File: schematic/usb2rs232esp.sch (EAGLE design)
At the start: 16 parts, among them IC2 FT232RL

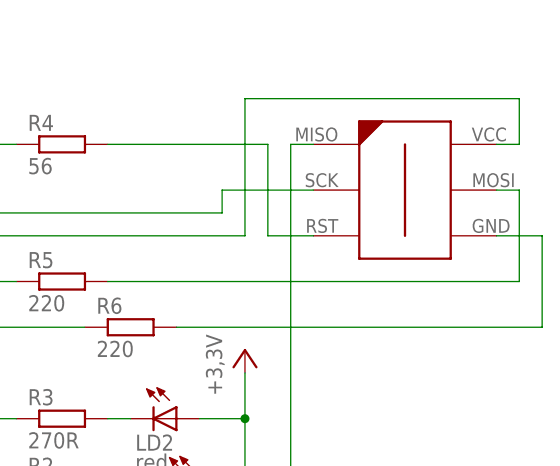
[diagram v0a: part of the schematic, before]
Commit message: improved lables
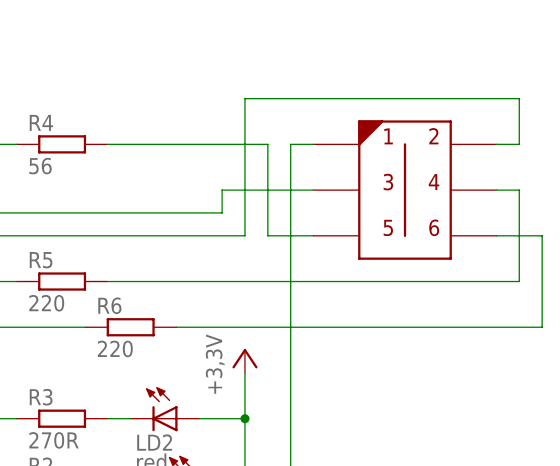
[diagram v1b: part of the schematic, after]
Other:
- note added: "1"
- note added: "2"
- note added: "3"
- note added: "4"
- note added: "5"
- note added: "6"
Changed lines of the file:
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@@
 <grid distance="0.1" unitdist="inch" unit="inch" style="lines" multiple="1" display="no" altdistance="0.01" altunitdist="inch" altunit="inch"/>
 <layers>
-<layer number="1" name="Top" color="4" fill="1" visible="yes" active="no"/>
-<layer number="2" name="Route2" color="3" fill="3" visible="yes" active="no"/>
-<layer number="3" name="Route3" color="5" fill="3" visible="yes" active="no"/>
-<layer number="4" name="Route4" color="1" fill="4" visible="yes" active="no"/>
-<layer number="5" name="Route5" color="4" fill="4" visible="yes" active="no"/>
-<layer number="6" name="Route6" color="1" fill="8" visible="yes" active="no"/>
-<layer number="7" name="Route7" color="4" fill="8" visible="yes" active="no"/>
-<layer number="8" name="Route8" color="1" fill="2" visible="yes" active="no"/>
-<layer number="9" name="Route9" color="4" fill="2" visible="yes" active="no"/>
-<layer number="10" name="Route10" color="1" fill="7" visible="yes" active="no"/>
-<layer number="11" name="Route11" color="4" fill="7" visible="yes" active="no"/>
-<layer number="12" name="Route12" color="1" fill="5" visible="yes" active="no"/>
-<layer number="13" name="Route13" color="4" fill="5" visible="yes" active="no"/>
-<layer number="14" name="Route14" color="1" fill="6" visible="yes" active="no"/>
-<layer number="15" name="Route15" color="4" fill="6" visible="yes" active="no"/>
-<layer number="16" name="Bottom" color="1" fill="1" visible="yes" active="no"/>
-<layer number="17" name="Pads" color="2" fill="1" visible="yes" active="no"/>
-<layer number="18" name="Vias" color="2" fill="1" visible="yes" active="no"/>
-<layer number="19" name="Unrouted" color="6" fill="1" visible="yes" active="no"/>
-<layer number="20" name="Dimension" color="15" fill="1" visible="yes" active="no"/>
-<layer number="21" name="tPlace" color="7" fill="1" visible="yes" active="no"/>
-<layer number="22" name="bPlace" color="7" fill="1" visible="yes" active="no"/>
-<layer number="23" name="tOrigins" color="15" fill="1" visible="yes" active="no"/>
-<layer number="24" name="bOrigins" color="15" fill="1" visible="yes" active="no"/>
-<layer number="25" name="tNames" color="7" fill="1" visible="yes" active="no"/>
-<layer number="26" name="bNames" color="7" fill="1" visible="yes" active="no"/>
-<layer number="27" name="tValues" color="7" fill="1" visible="yes" active="no"/>
-<layer number="28" name="bValues" color="7" fill="1" visible="yes" active="no"/>
+<layer number="1" name="Top" color="4" fill="1" visible="no" active="no"/>
+<layer number="2" name="Route2" color="3" fill="3" visible="no" active="no"/>
+<layer number="3" name="Route3" color="5" fill="3" visible="no" active="no"/>
+<layer number="4" name="Route4" color="1" fill="4" visible="no" active="no"/>
+<layer number="5" name="Route5" color="4" fill="4" visible="no" active="no"/>
+<layer number="6" name="Route6" color="1" fill="8" visible="no" active="no"/>
+<layer number="7" name="Route7" color="4" fill="8" visible="no" active="no"/>
+<layer number="8" name="Route8" color="1" fill="2" visible="no" active="no"/>
+<layer number="9" name="Route9" color="4" fill="2" visible="no" active="no"/>
+<layer number="10" name="Route10" color="1" fill="7" visible="no" active="no"/>
+<layer number="11" name="Route11" color="4" fill="7" visible="no" active="no"/>
+<layer number="12" name="Route12" color="1" fill="5" visible="no" active="no"/>
+<layer number="13" name="Route13" color="4" fill="5" visible="no" active="no"/>
+<layer number="14" name="Route14" color="1" fill="6" visible="no" active="no"/>
+<layer number="15" name="Route15" color="4" fill="6" visible="no" active="no"/>
+<layer number="16" name="Bottom" color="1" fill="1" visible="no" active="no"/>
+<layer number="17" name="Pads" color="2" fill="1" visible="no" active="no"/>
+<layer number="18" name="Vias" color="2" fill="1" visible="no" active="no"/>
+<layer number="19" name="Unrouted" color="6" fill="1" visible="no" active="no"/>
+<layer number="20" name="Dimension" color="15" fill="1" visible="no" active="no"/>
+<layer number="21" name="tPlace" color="7" fill="1" visible="no" active="no"/>
+<layer number="22" name="bPlace" color="7" fill="1" visible="no" active="no"/>
+<layer number="23" name="tOrigins" color="15" fill="1" visible="no" active="no"/>
+<layer number="24" name="bOrigins" color="15" fill="1" visible="no" active="no"/>
+<layer number="25" name="tNames" color="7" fill="1" visible="no" active="no"/>
+<layer number="26" name="bNames" color="7" fill="1" visible="no" active="no"/>
+<layer number="27" name="tValues" color="7" fill="1" visible="no" active="no"/>
+<layer number="28" name="bValues" color="7" fill="1" visible="no" active="no"/>
 <layer number="29" name="tStop" color="7" fill="3" visible="no" active="no"/>
 <layer number="30" name="bStop" color="7" fill="6" visible="no" active="no"/>
@@
 <layer number="35" name="tGlue" color="7" fill="4" visible="no" active="no"/>
 <layer number="36" name="bGlue" color="7" fill="5" visible="no" active="no"/>
-<layer number="37" name="tTest" color="7" fill="1" visible="yes" active="no"/>
-<layer number="38" name="bTest" color="7" fill="1" visible="yes" active="no"/>
+<layer number="37" name="tTest" color="7" fill="1" visible="no" active="no"/>
+<layer number="38" name="bTest" color="7" fill="1" visible="no" active="no"/>
 <layer number="39" name="tKeepout" color="4" fill="11" visible="no" active="no"/>
 <layer number="40" name="bKeepout" color="1" fill="11" visible="no" active="no"/>
@@
 <layer number="44" name="Drills" color="7" fill="1" visible="no" active="no"/>
 <layer number="45" name="Holes" color="7" fill="1" visible="no" active="no"/>
-<layer number="46" name="Milling" color="3" fill="1" visible="yes" active="no"/>
-<layer number="47" name="Measures" color="7" fill="1" visible="yes" active="no"/>
-<layer number="48" name="Document" color="7" fill="1" visible="yes" active="no"/>
-<layer number="49" name="Reference" color="7" fill="1" visible="yes" active="no"/>
-<layer number="50" name="dxf" color="7" fill="1" visible="yes" active="no"/>
-<layer number="51" name="tDocu" color="7" fill="1" visible="yes" active="no"/>
-<layer number="52" name="bDocu" color="7" fill="1" visible="yes" active="no"/>
-<layer number="53" name="tGND_GNDA" color="7" fill="9" visible="yes" active="no"/>
-<layer number="54" name="bGND_GNDA" color="1" fill="9" visible="yes" active="no"/>
-<layer number="56" name="wert" color="7" fill="1" visible="yes" active="no"/>
+<layer number="46" name="Milling" color="3" fill="1" visible="no" active="no"/>
+<layer number="47" name="Measures" color="7" fill="1" visible="no" active="no"/>
+<layer number="48" name="Document" color="7" fill="1" visible="no" active="no"/>
+<layer number="49" name="Reference" color="7" fill="1" visible="no" active="no"/>
+<layer number="50" name="dxf" color="7" fill="1" visible="no" active="no"/>
+<layer number="51" name="tDocu" color="7" fill="1" visible="no" active="no"/>
+<layer number="52" name="bDocu" color="7" fill="1" visible="no" active="no"/>
+<layer number="53" name="tGND_GNDA" color="7" fill="9" visible="no" active="no"/>
+<layer number="54" name="bGND_GNDA" color="1" fill="9" visible="no" active="no"/>
+<layer number="56" name="wert" color="7" fill="1" visible="no" active="no"/>
 <layer number="91" name="Nets" color="2" fill="1" visible="yes" active="yes"/>
 <layer number="92" name="Busses" color="1" fill="1" visible="yes" active="yes"/>
@@
 5 Vout (3V3)
 6 GPIO0</text>
+<text x="144.78" y="81.28" size="1.778" layer="94">1</text>
+<text x="149.86" y="81.28" size="1.778" layer="94">2</text>
+<text x="144.78" y="76.2" size="1.778" layer="94">3</text>
+<text x="149.86" y="76.2" size="1.778" layer="94">4</text>
+<text x="144.78" y="71.12" size="1.778" layer="94">5</text>
+<text x="149.86" y="71.12" size="1.778" layer="94">6</text>
 </plain>
 <instances>
@@
 <instance part="GND9" gate="1" x="60.96" y="15.24"/>
 <instance part="U$40" gate="G$1" x="15.24" y="38.1" rot="MR0"/>
-<instance part="U$3" gate="G$1" x="147.32" y="76.2"/>
+<instance part="U$3" gate="G$1" x="147.32" y="76.2" smashed="yes"/>
 <instance part="GND4" gate="1" x="134.62" y="15.24"/>
 <instance part="R4" gate="G$1" x="109.22" y="81.28"/>
